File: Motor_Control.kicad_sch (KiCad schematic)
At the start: 4 parts, among them J15 Motor2 encoder, J16 MDD20A PWM2/DIR2/GND, J6 MDD20A PWM1/DIR1/GND, J7 Motor1 encoder

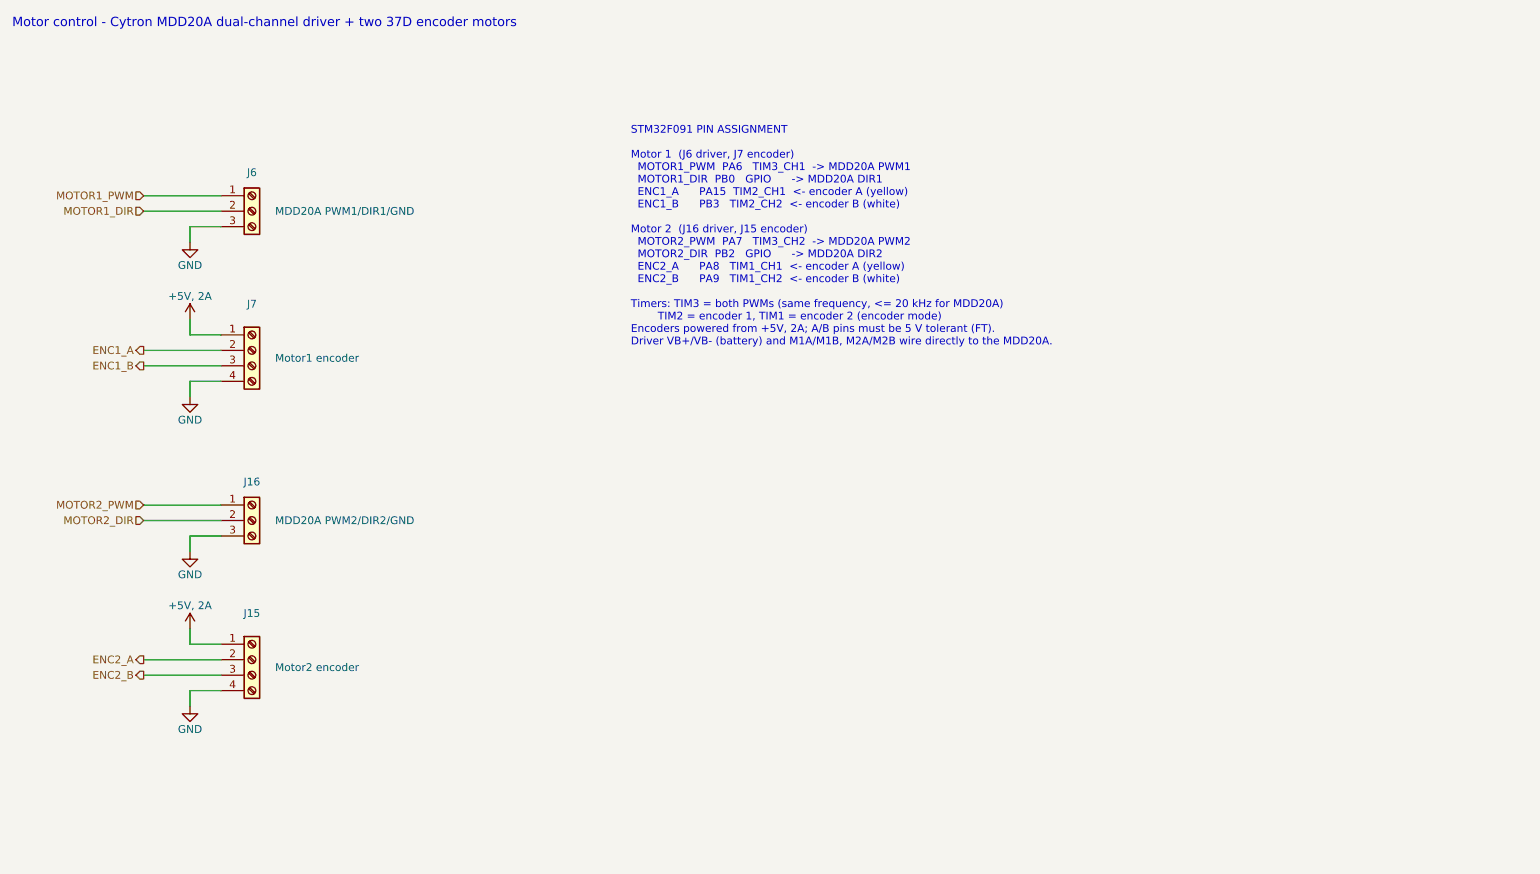
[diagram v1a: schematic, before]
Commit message: Add series resistors on off-board signals and ESD arrays on J6/J7
Series protection (100R 0805, near U1, matching R12/R13 on the Pi UART)
on every off-board control and encoder line. Each line is split into
an MCU-side net and a connector-side *_CONN net:
- R26/R27 MOTOR1_PWM/DIR (J6), R28/R29 ENC1_A/B (J7)
- R30/R31 MOTOR2_PWM/DIR (J16), R32/R33 ENC2_A/B (J15)
- R34/R35 IMU_INT/RST (J12)

ESD arrays (populated) on motor 1 only, ST USBLC6-4SC6 in SOT-23-6
for hand soldering:
- U6 on J6 PWM/DIR, VBUS +3V3, C34 100 nF
- U7 on J7 encoder A/B, VBUS +5V 2A (the encoder supply), C35 100 nF
Spare channels are no-connect.

Move the IMU block (J11, J12, DNP pull-ups R10/R11) from the root
sheet to a new IMU_Interface.kicad_sch sheet (page 11) to make room for
R34/R35. It connects by global labels and has a pin note on the root
block. Update the motor pin table and the README.
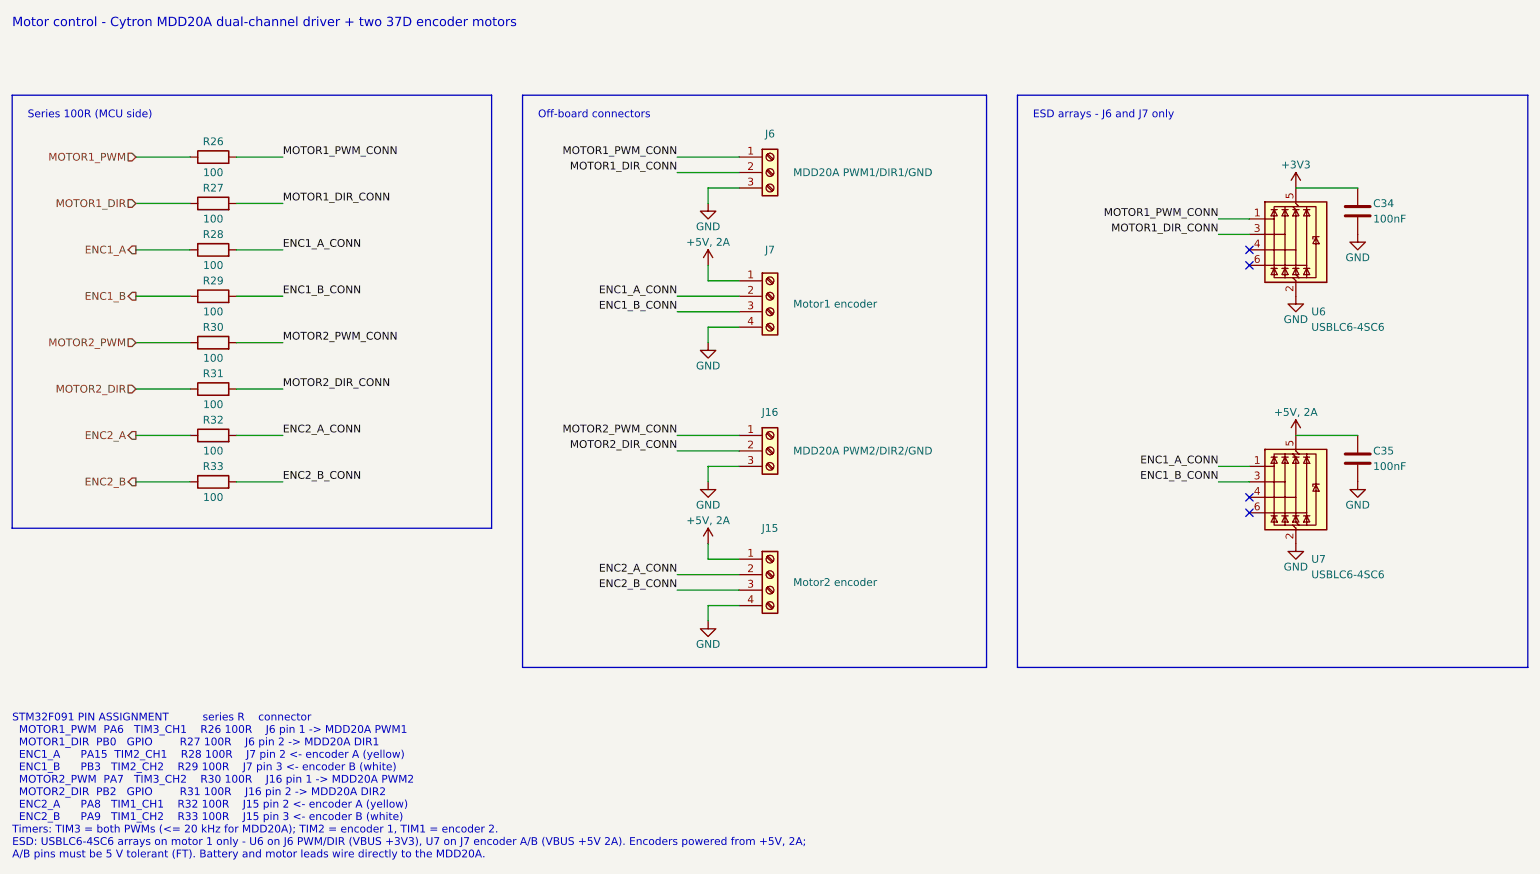
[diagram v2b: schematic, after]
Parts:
- added C34, C35: 100nF, Capacitor_SMD:C_0603_1608Metric, symbol Device:C
- added R26, R27, R28, R29, R30, R31, R32, R33: 100, Resistor_SMD:R_0805_2012Metric, symbol Device:R
- added U6, U7: USBLC6-4SC6, Package_TO_SOT_SMD:SOT-23-6, symbol Power_Protection:USBLC6-4SC6
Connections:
- net +5V, 2A: now also C35.1, U7.5 (VBUS)
- net ENC1_A: now also R28.1; no longer J7.2 (Pin_2)
- net ENC1_B: now also R29.1; no longer J7.3 (Pin_3)
- net ENC2_A: now also R32.1; no longer J15.2 (Pin_2)
- net ENC2_B: now also R33.1; no longer J15.3 (Pin_3)
- net GND: now also C34.2, C35.2, U6.2 (GND), U7.2 (GND)
- net MOTOR1_DIR: now also R27.1; no longer J6.2 (Pin_2)
- net MOTOR1_PWM: now also R26.1; no longer J6.1 (Pin_1)
- net MOTOR2_DIR: now also R31.1; no longer J16.2 (Pin_2)
- net MOTOR2_PWM: now also R30.1; no longer J16.1 (Pin_1)
- new net +3V3: C34.1, U6.5 (VBUS)
- new net ENC1_A_CONN: J7.2 (Pin_2), R28.2, U7.1 (I/O1)
- new net ENC1_B_CONN: J7.3 (Pin_3), R29.2, U7.3 (I/O2)
- new net ENC2_A_CONN: J15.2 (Pin_2), R32.2
- new net ENC2_B_CONN: J15.3 (Pin_3), R33.2
- new net MOTOR1_DIR_CONN: J6.2 (Pin_2), R27.2, U6.3 (I/O2)
- new net MOTOR1_PWM_CONN: J6.1 (Pin_1), R26.2, U6.1 (I/O1)
- new net MOTOR2_DIR_CONN: J16.2 (Pin_2), R31.2
- new net MOTOR2_PWM_CONN: J16.1 (Pin_1), R30.2
- no-connect marks 0 -> 4
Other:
- note added: "ESD arrays - J6 and J7 only"
- note added: "Off-board connectors"
- note added: "STM32F091 PIN ASSIGNMENT series R connector MOTOR1_PWM PA6 TIM3_CH1 R26 100R J6 pin 1 -> MDD20A PWM1 MOTOR1_DIR PB0 GPIO R27 100R J6 pin 2 -> MDD20A DIR1 ENC1_A PA15 TIM2_CH1 R28 100R J7 pin 2 <- encoder A (yellow) ENC1_B PB3 TIM2_CH2 R29 100R J7 pin 3 <- encoder B (white) MOTOR2_PWM PA7 TIM3_CH2 R30 100R J16 pin 1 -> MDD20A PWM2 MOTOR2_DIR PB2 GPIO R31 100R J16 pin 2 -> MDD20A DIR2 ENC2_A PA8 TI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"
- note added: "Series 100R (MCU side)"
- note removed: "STM32F091 PIN ASSIGNMENT Motor 1 (J6 driver, J7 encoder) MOTOR1_PWM PA6 TIM3_CH1 -> MDD20A PWM1 MOTOR1_DIR PB0 GPIO -> MDD20A DIR1 ENC1_A PA15 TIM2_CH1 <- encoder A (yellow) ENC1_B PB3 TIM2_CH2 <- encoder B (white) Motor 2 (J16 driver, J15 encoder) MOTOR2_PWM PA7 TIM3_CH2 -> MDD20A PWM2 MOTOR2_DIR PB2 GPIO -> MDD20A DIR2 ENC2_A PA8 TIM1_CH1 <- encoder A (yellow) ENC2_B PA9 TIM1_CH2 <- encoder B (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"
- moved on the sheet: J15, J16, J6, J7
